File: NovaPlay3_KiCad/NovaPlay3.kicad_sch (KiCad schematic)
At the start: 0 parts

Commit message: Started schematic
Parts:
- added R1, R2, R3: 10K, symbol Device:R
- added U1: ESP32-S3-WROOM-1, RF_Module:ESP32-S3-WROOM-1, symbol RF_Module:ESP32-S3-WROOM-1
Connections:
- new net: R3.2, U1.27 (IO0)
- new net: R2.2, U1.15 (IO3)
- new net: R1.2, U1.3 (EN)
- new net +3.3V: R1.1, R2.1, R3.1, U1.2 (3V3)
- new net GND: U1.1 (GND), U1.40 (GND), U1.41 (GND)
- new net USB_D+: U1.14 (USB_D+)
- new net USB_D-: U1.13 (USB_D-)
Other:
- added sheet Power Management (Power_management.kicad_sch)

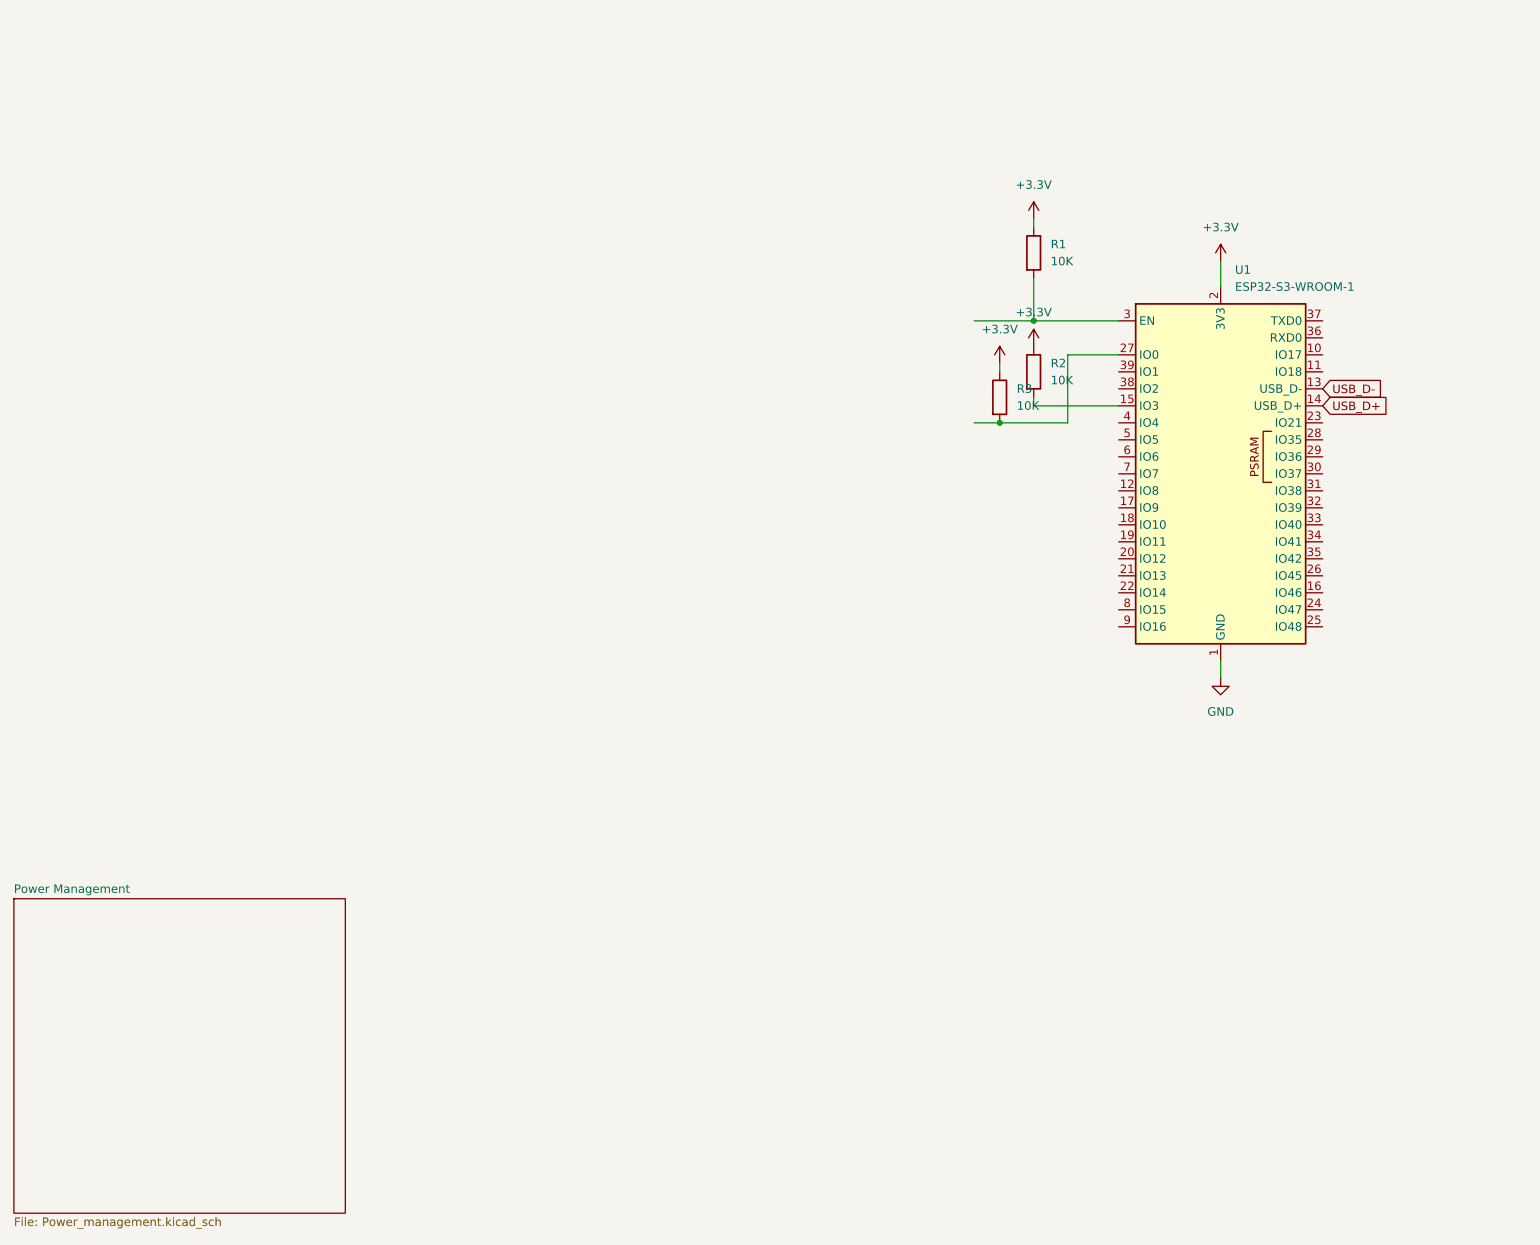
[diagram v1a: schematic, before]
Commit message: Added new sheets
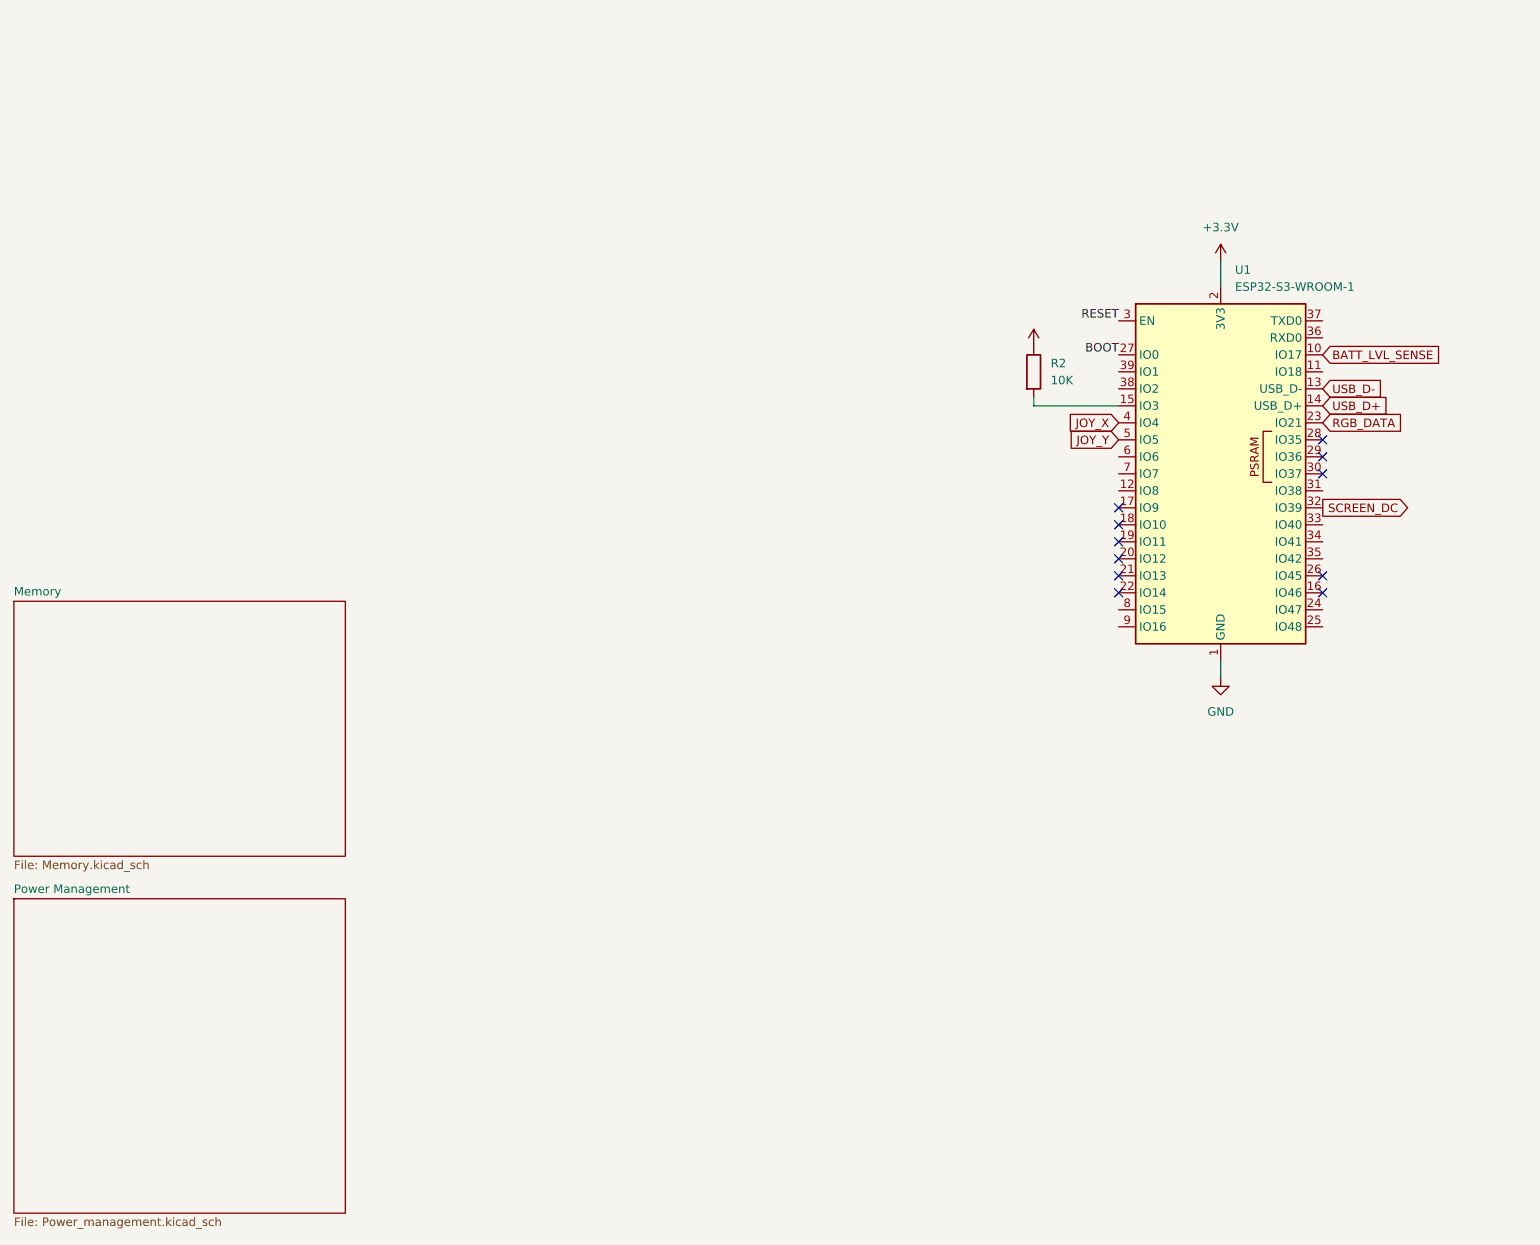
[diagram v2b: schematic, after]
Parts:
- removed R1, R3: 10K, symbol Device:R
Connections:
- net BOOT: now reaches U1.27 (IO0)
- net BATT_LVL_SENSE: now reaches U1.10 (IO17)
- net RGB_DATA: now reaches U1.23 (IO21)
- net RESET: now reaches U1.3 (EN)
- net JOY_X: now reaches U1.4 (IO4)
- net JOY_Y: now reaches U1.5 (IO5)
- no-connect marks 0 -> 11
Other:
- added sheet Memory (Memory.kicad_sch)

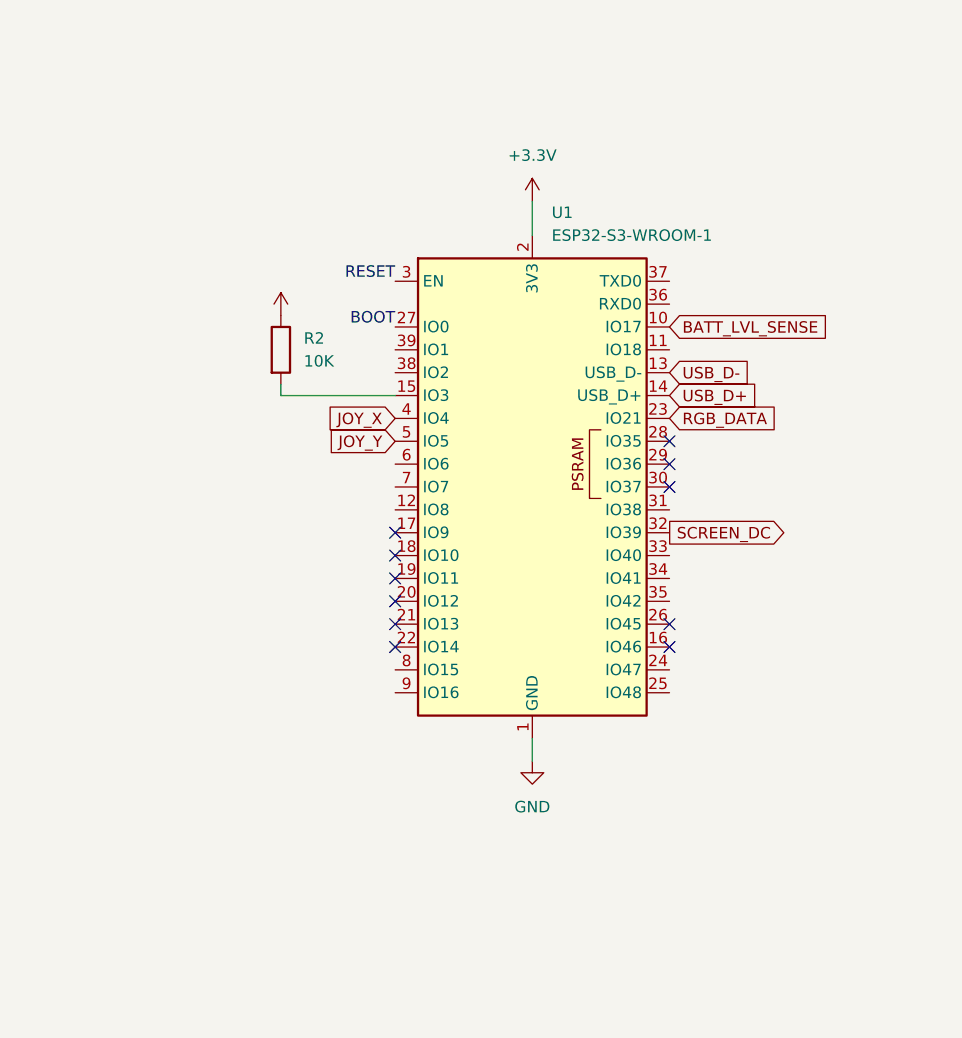
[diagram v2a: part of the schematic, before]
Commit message: Finished power management
power management schematic is done
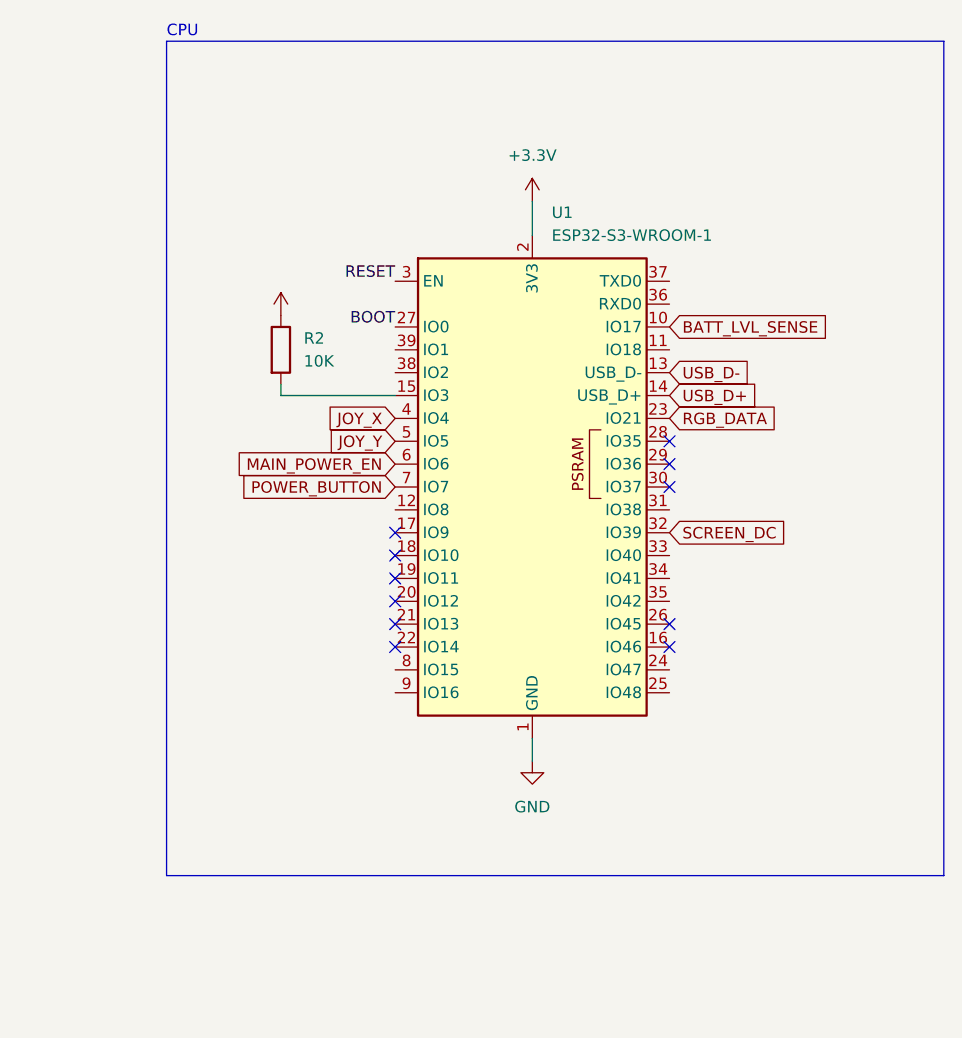
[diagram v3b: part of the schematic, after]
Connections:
- net SCREEN_DC: now also U1.32 (IO39)
- net MAIN_POWER_EN: now reaches U1.6 (IO6)
- net POWER_BUTTON: now reaches U1.7 (IO7)
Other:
- note added: "CPU"
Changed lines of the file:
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@@
 	(generator_version "9.0")
 	(paper "A4")
+	(rectangle
+		(start 154.94 33.02)
+		(end 241.3 125.73)
+		(stroke
+			(width 0)
+			(type default)
+		)
+		(fill
+			(type none)
+		)
+	)
+	(text "CPU"
+		(exclude_from_sim no)
+		(at 156.718 32.004 0)
+		(effects
+			(font
+				(size 1.27 1.27)
+			)
+		)
+	)
 	(no_connect
 		(at 180.34 100.33)
@@
 		)
 	)
+	(global_label "POWER_BUTTON"
+		(shape input)
+		(at 180.34 82.55 180)
+		(fields_autoplaced yes)
+		(effects
+			(font
+				(size 1.27 1.27)
+			)
+			(justify right)
+		)
+		(property "Intersheetrefs" "${INTERSHEET_REFS}"
+			(at 162.7196 82.55 0)
+			(effects
+				(font
+					(size 1.27 1.27)
+				)
+				(justify right)
+				(hide yes)
+			)
+		)
+	)
+	(global_label "MAIN_POWER_EN"
+		(shape input)
+		(at 180.34 80.01 180)
+		(fields_autoplaced yes)
+		(effects
+			(font
+				(size 1.27 1.27)
+			)
+			(justify right)
+		)
+		(property "Intersheetrefs" "${INTERSHEET_REFS}"
+			(at 161.9939 80.01 0)
+			(effects
+				(font
+					(size 1.27 1.27)
+				)
+				(justify right)
+				(hide yes)
+			)
+		)
+	)
 	(global_label "BATT_LVL_SENSE"
 		(shape input)
@@
 	(global_label "SCREEN_DC"
 		(shape input)
-		(at 223.52 87.63 180)
-		(fields_autoplaced yes)
-		(effects
-			(font
-				(size 1.27 1.27)
-			)
-			(justify right)
-		)
-		(property "Intersheetrefs" "${INTERSHEET_REFS}"
-			(at 209.6492 87.63 0)
-			(effects
-				(font
-					(size 1.27 1.27)
-				)
-				(justify right)
-				(hide yes)
-			)
+		(at 210.82 87.63 0)
+		(fields_autoplaced yes)
+		(effects
+			(font
+				(size 1.27 1.27)
+			)
+			(justify left)
+		)
+		(property "Intersheetrefs" "${INTERSHEET_REFS}"
+			(at 224.6908 87.63 0)
+			(effects
+				(font
+					(size 1.27 1.27)
+				)
+				(justify left)
+				(hide yes)
+			)

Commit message: Sync
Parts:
- renumbered R2 to R1
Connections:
- net SCREEN_DC: now also U1.31 (IO38); no longer U1.32 (IO39)
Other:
- added sheet Buttons & other inputs (userinputs.kicad_sch)
- added sheet Screen & other outputs (useroutputs.kicad_sch)
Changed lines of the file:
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@@
 	(global_label "SCREEN_DC"
 		(shape input)
-		(at 210.82 87.63 0)
+		(at 210.82 85.09 0)
 		(fields_autoplaced yes)
 		(effects
@@
 		)
 		(property "Intersheetrefs" "${INTERSHEET_REFS}"
-			(at 224.6908 87.63 0)
+			(at 224.6908 85.09 0)
 			(effects
 				(font
@@
 		(dnp no)
 		(fields_autoplaced yes)
-		(property "Reference" "#PWR01"
+		(property "Reference" "#PWR03"
 			(at 195.58 119.38 0)
 			(effects
@@
 			(project ""
 				(path "/3902e32d-76e7-44cb-8277-c0e17db8d088"
-					(reference "#PWR01")
+					(reference "#PWR03")
 					(unit 1)
 				)
@@
 		(dnp no)
 		(fields_autoplaced yes)
-		(property "Reference" "#PWR04"
+		(property "Reference" "#PWR02"
 			(at 167.64 67.31 0)
 			(effects
@@
 			(project "NovaPlay3"
 				(path "/3902e32d-76e7-44cb-8277-c0e17db8d088"
-					(reference "#PWR04")
+					(reference "#PWR02")
 					(unit 1)
 				)
@@
 		(dnp no)
 		(fields_autoplaced yes)
-		(property "Reference" "R2"
+		(property "Reference" "R1"
 			(at 170.18 66.0399 0)
 			(effects
@@
 			(project "NovaPlay3"
 				(path "/3902e32d-76e7-44cb-8277-c0e17db8d088"
-					(reference "R2")
+					(reference "R1")
 					(unit 1)
 				)
@@
 		(dnp no)
 		(fields_autoplaced yes)
-		(property "Reference" "#PWR02"
+		(property "Reference" "#PWR01"
 			(at 195.58 54.61 0)
 			(effects
@@
 			(project ""
 				(path "/3902e32d-76e7-44cb-8277-c0e17db8d088"
-					(reference "#PWR02")
+					(reference "#PWR01")
 					(unit 1)
 				)
 			)
+		)
+	)
+	(sheet
+		(at 15.24 62.23)
+		(size 49.53 33.02)
+		(exclude_from_sim no)
+		(in_bom yes)
+		(on_board yes)
+		(dnp no)
+		(fields_autoplaced yes)
+		(stroke
+			(width 0.1524)
+			(type solid)
+		)
+		(fill
+			(color 0 0 0 0.0000)
+		)
+		(property "Sheetname" "Buttons & other inputs"
+			(at 15.24 61.5184 0)
+			(effects
+				(font
+					(size 1.27 1.27)
+				)
+				(justify left bottom)
+			)
+		)
+		(property "Sheetfile" "userinputs.kicad_sch"
+			(at 15.24 95.8346 0)
+			(effects
+				(font
+					(size 1.27 1.27)
+				)
+				(justify left top)
+			)
+		)
+		(instances
+			(project "NovaPlay3"
+				(path "/3902e32d-76e7-44cb-8277-c0e17db8d088"
+					(page "4")
+				)
+			)
+		)
+	)
+	(sheet
+		(at 15.24 16.51)
+		(size 49.53 40.64)
+		(exclude_from_sim no)
+		(in_bom yes)
+		(on_board yes)
+		(dnp no)
+		(fields_autoplaced yes)
+		(stroke
+			(width 0.1524)
+			(type solid)
+		)
+		(fill
+			(color 0 0 0 0.0000)
+		)
+		(property "Sheetname" "Screen & other outputs"
+			(at 15.24 15.7984 0)
+			(effects
+				(font
+					(size 1.27 1.27)
+				)
+				(justify left bottom)
+			)
+		)
+		(property "Sheetfile" "useroutputs.kicad_sch"
+			(at 15.24 57.7346 0)
+			(effects
+				(font
+					(size 1.27 1.27)
+				)
+				(justify left top)
+			)
+		)
+		(instances
+			(project "NovaPlay3"
+				(path "/3902e32d-76e7-44cb-8277-c0e17db8d088"
+					(page "5")
+				)
+			)
